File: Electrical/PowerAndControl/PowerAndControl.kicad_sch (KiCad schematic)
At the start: 21 parts, among them J1 Conn_02x03_Counter_Clockwise, SW2 SW_SPDT_312, U1 MCP73811T-420I-OT, U2 TPS22919QDCKRQ1, U3 TPS3840PL30DBVR

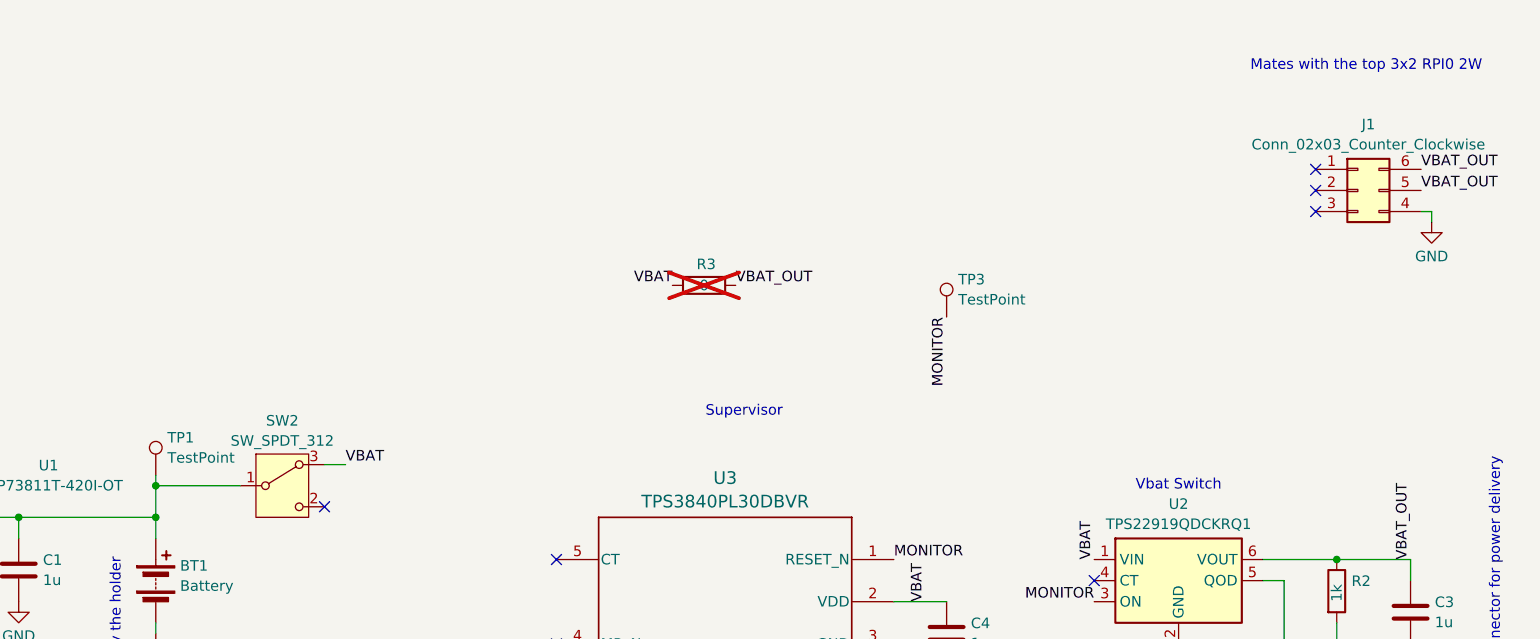
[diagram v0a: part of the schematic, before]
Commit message: Layout of AA variant complete.  Need to check pinout 2x more
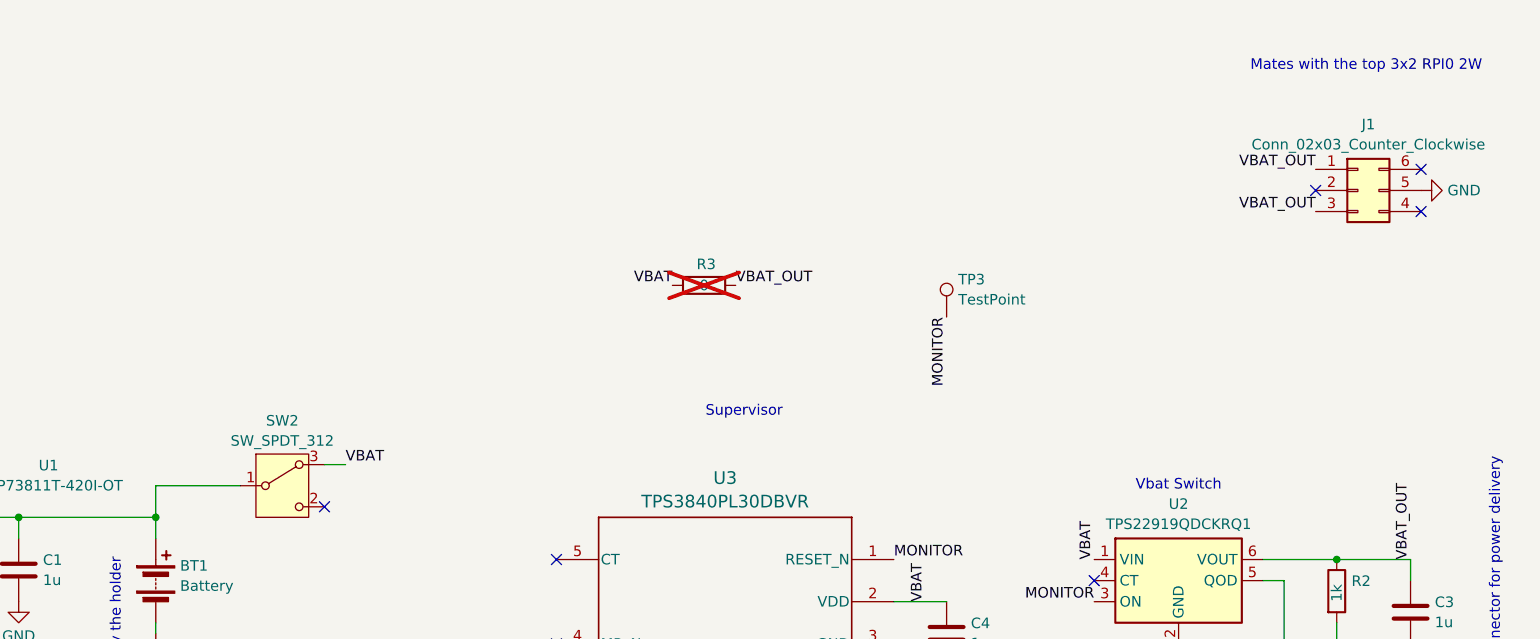
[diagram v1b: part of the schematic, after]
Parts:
- removed TP1: TestPoint, TestPoint:TestPoint_Pad_1.0x1.0mm, symbol Connector:TestPoint
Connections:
- net GND: now also J1.5 (Pin_5); no longer J1.4 (Pin_4)
- net VBAT_OUT: now also J1.1 (Pin_1), J1.3 (Pin_3); no longer J1.5 (Pin_5), J1.6 (Pin_6)
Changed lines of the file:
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@@
-		(color 0 0 0 0)
-	)
-	(junction
-		(at 115.57 107.95)
-		(diameter 0)
 		(color 0 0 0 0)
 	)
@@
 	)
 	(no_connect
-		(at 255.27 72.39)
-	)
-	(no_connect
 		(at 135.89 110.49)
 	)
@@
 	)
 	(no_connect
-		(at 255.27 69.85)
+		(at 267.97 74.93)
 	)
 	(no_connect
@@
 	)
 	(no_connect
-		(at 255.27 74.93)
+		(at 255.27 72.39)
 	)
 	(no_connect
@@
 	)
 	(no_connect
+		(at 267.97 69.85)
+	)
+	(no_connect
 		(at 163.83 116.84)
 	)
@@
 	(wire
 		(pts
-			(xy 269.24 74.93) (xy 269.24 76.2)
-		)
-		(stroke
-			(width 0)
-			(type default)
-		)
-	)
-	(wire
-		(pts
 			(xy 266.7 116.84) (xy 266.7 119.38)
 		)
@@
 	(wire
 		(pts
-			(xy 115.57 106.68) (xy 115.57 107.95)
-		)
-		(stroke
-			(width 0)
-			(type default)
-		)
-	)
-	(wire
-		(pts
 			(xy 43.18 97.79) (xy 43.18 95.25)
 		)
@@
 		(pts
 			(xy 138.43 105.41) (xy 135.89 105.41)
-		)
-		(stroke
-			(width 0)
-			(type default)
-		)
-	)
-	(wire
-		(pts
-			(xy 267.97 74.93) (xy 269.24 74.93)
 		)
 		(stroke
@@
 		)
 	)
-	(label "VBAT_OUT"
-		(at 267.97 72.39 0)
-		(effects
-			(font
-				(size 1.27 1.27)
-			)
-			(justify left bottom)
-		)
-	)
 	(label "VBAT"
 		(at 208.28 121.92 90)
@@
 		)
 	)
+	(label "VBAT_OUT"
+		(at 255.27 69.85 180)
+		(effects
+			(font
+				(size 1.27 1.27)
+			)
+			(justify right bottom)
+		)
+	)
+	(label "VBAT_OUT"
+		(at 255.27 74.93 180)
+		(effects
+			(font
+				(size 1.27 1.27)
+			)
+			(justify right bottom)
+		)
+	)
 	(label "MONITOR"
 		(at 204.47 116.84 0)
@@
 		)
 	)
-	(label "VBAT_OUT"
-		(at 267.97 69.85 0)
-		(effects
-			(font
-				(size 1.27 1.27)
-			)
-			(justify left bottom)
-		)
-	)
 	(symbol
 		(lib_id "power:GND")
@@
 	(symbol
 		(lib_id "power:GND")
-		(at 269.24 76.2 0)
+		(at 267.97 72.39 90)
 		(unit 1)
 		(exclude_from_sim no)
@@
 		(fields_autoplaced yes)
 		(property "Reference" "#PWR017"
-			(at 269.24 82.55 0)
+			(at 274.32 72.39 0)
 			(effects
 				(font
@@
 		)
 		(property "Value" "GND"
-			(at 269.24 80.3331 0)
-			(effects
-				(font
-					(size 1.27 1.27)
-				)
+			(at 271.145 72.39 90)
+			(effects
+				(font
+					(size 1.27 1.27)
+				)
+				(justify right)
 			)
 		)
 		(property "Footprint" ""
-			(at 269.24 76.2 0)
+			(at 267.97 72.39 0)
 			(effects
 				(font
@@
 		)
 		(property "Datasheet" ""
-			(at 269.24 76.2 0)
+			(at 267.97 72.39 0)
 			(effects
 				(font
@@
 		)
 		(property "Description" "Power symbol creates a global label with name \"GND\" , ground"
-			(at 269.24 76.2 0)
-			(effects
-				(font
-					(size 1.27 1.27)
-				)
-				(hide yes)
-			)
-		)
-		(pin "1"
-		)
-		(instances
-			(project ""
+			(at 267.97 72.39 0)
+			(effects
+				(font
+					(size 1.27 1.27)
+				)
+				(hide yes)
+			)
+		)
+		(pin "1"
+		)
+		(instances
+			(project "PowerAndControl"
 				(path "/a4a2b9eb-fb12-482a-8327-284239d2fb85"
 					(reference "#PWR017")
 					(unit 1)
 				)
-			)
-		)
-	)
-	(symbol
-		(lib_id "Connector:TestPoint")
-		(at 115.57 106.68 0)
-		(unit 1)
-		(exclude_from_sim no)
-		(in_bom yes)
-		(on_board yes)
-		(dnp no)
-		(property "Reference" "TP1"
-			(at 116.967 102.1658 0)
-			(effects
-				(font
-					(size 1.27 1.27)
-				)
-				(justify left)
-			)
-		)
-		(property "Value" "TestPoint"
-			(at 116.967 104.5901 0)
-			(effects
-				(font
-					(size 1.27 1.27)
-				)
-				(justify left)
-			)
-		)
-		(property "Footprint" "TestPoint:TestPoint_Pad_1.0x1.0mm"
-			(at 120.65 106.68 0)
-			(effects
-				(font
-					(size 1.27 1.27)
-				)
-				(hide yes)
-			)
-		)
-		(property "Datasheet" "~"
-			(at 120.65 106.68 0)
-			(effects
-				(font
-					(size 1.27 1.27)
-				)
-				(hide yes)
-			)
-		)
-		(property "Description" "test point"
-			(at 115.57 106.68 0)
-			(effects
-				(font
-					(size 1.27 1.27)
-				)
-				(hide yes)
-			)
-		)
-		(pin "1"
-		)
-		(instances
-			(project ""
-				(path "/a4a2b9eb-fb12-482a-8327-284239d2fb85"
-					(reference "TP1")
-					(unit 1)
-				)

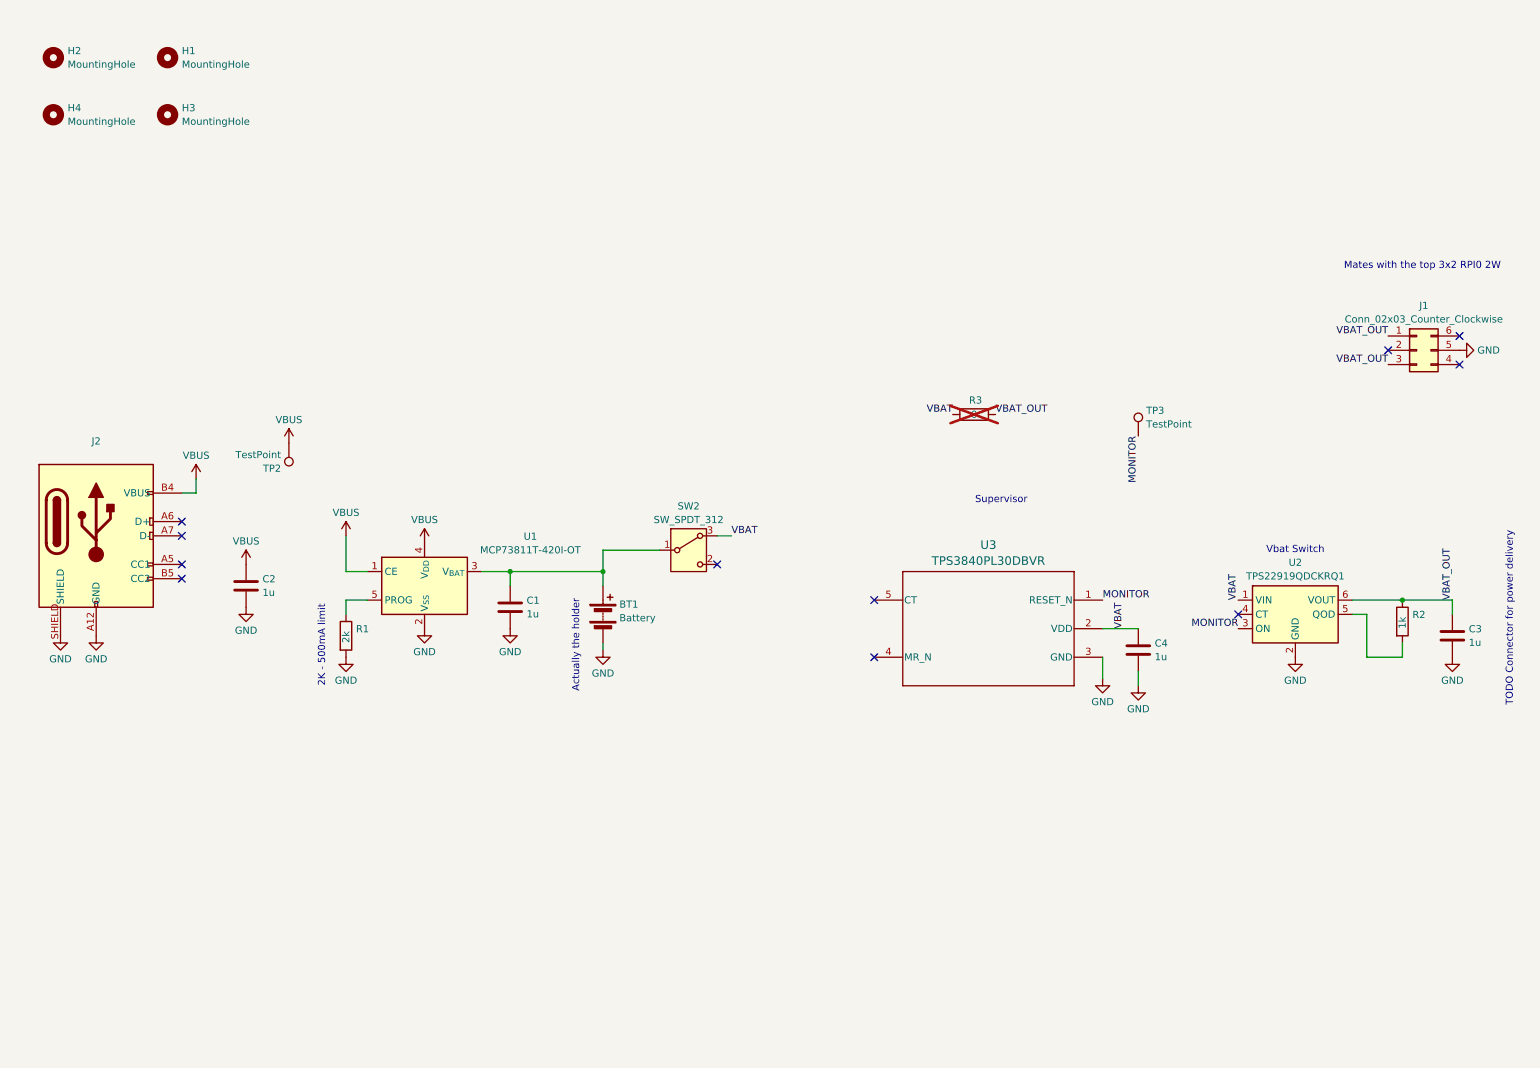
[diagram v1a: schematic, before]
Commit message: Cleaner Schematic / LED Indicators, better Layout
Added 3 LEDs for indicators.
Shcematic Cleaned up in general.
New Charger component
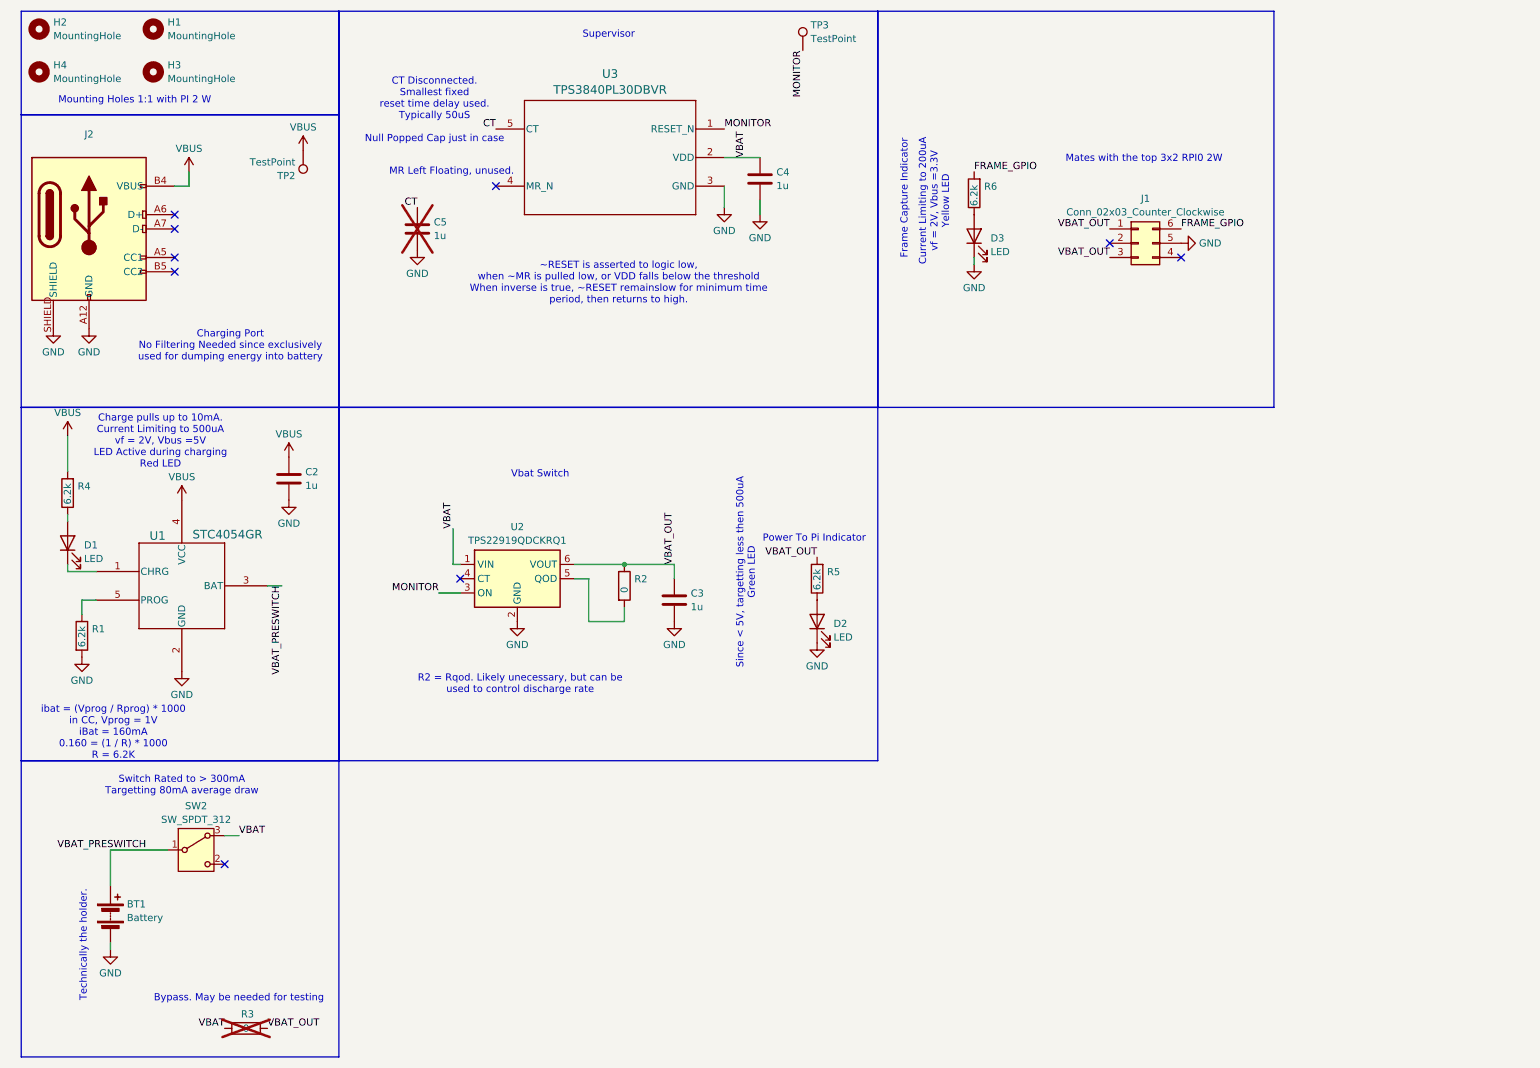
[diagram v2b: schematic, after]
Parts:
- removed C1: 1u, Capacitor_SMD:C_0402_1005Metric_Pad0.74x0.62mm_HandSolder, symbol Device:C
- removed U1: MCP73811T-420I-OT, Package_TO_SOT_SMD:SOT-23-5, symbol Battery_Management:MCP73811T-420I-OT
- added C5: 1u, Capacitor_SMD:C_0603_1608Metric_Pad1.08x0.95mm_HandSolder, symbol Device:C
- added D1, D2, D3: LED, Library:LED_0604, symbol Device:LED
- added R4, R5, R6: 6.2k, Resistor_SMD:R_0402_1005Metric_Pad0.72x0.64mm_HandSolder, symbol Device:R
- added U1: STC4054GR, Package_TO_SOT_SMD:TSOT-23-5_HandSoldering, symbol New_Library:STC4054GR
- BT1: MPN  (none) -> BAT_BK-53
- R1: value 2k -> 6.2k
- R2: value 1k -> 0
- SW2: MPN (none) -> EGJ1210
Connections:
- net GND: now also C5.2, D2.1 (K), D3.1 (K), U1.2 (GND)
- net VBAT_OUT: now also R5.2
- net VBUS: now also R4.2, U1.4 (VCC)
- net at R1.1: now also U1.5 (PROG)
- net FRAME_GPIO: now reaches J1.6 (Pin_6)
- net FRAME_GPIO: now also R6.2
- net CT: now reaches U3.5 (CT)
- net CT: now also C5.1
- net VBAT_PRESWITCH: now reaches BT1.1 (+), SW2.1 (B)
- net VBAT_PRESWITCH: now also U1.3 (BAT)
- new net: D1.1 (K), U1.1 (CHRG)
- new net: D1.2 (A), R4.1
- new net: D3.2 (A), R6.1
- new net: D2.2 (A), R5.1
- no-connect marks 11 -> 9
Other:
- note added: "Bypass. May be needed for testing"
- note added: "CT Disconnected. Smallest fixed reset time delay used. Typically 50uS Null Popped Cap just in case"
- note added: "Charge pulls up to 10mA. Current Limiting to 500uA vf = 2V, Vbus =5V LED Active during charging Red LED"
- note added: "Charging Port No Filtering Needed since exclusively used for dumping energy into battery"
- note added: "Current Limiting to 200uA vf = 2V, Vbus =3.3V Yellow LED"
- note added: "Frame Capture Indicator"
- note added: "MR Left Floating, unused."
- note added: "Mounting Holes 1:1 with PI 2 W"
- note added: "Power To Pi Indicator"
- note added: "R2 = Rqod. Likely unecessary, but can be used to control discharge rate"
- note added: "Since < 5V, targetting less then 500uA Green LED"
- note added: "Switch Rated to > 300mA Targetting 80mA average draw"
- note added: "Technically the holder."
- note added: "ibat = (Vprog / Rprog) * 1000 in CC, Vprog = 1V iBat = 160mA 0.160 = (1 / R) * 1000 R = 6.2K"
- note added: "~RESET is asserted to logic low, when ~MR is pulled low, or VDD falls below the threshold When inverse is true, ~RESET remainslow for minimum time period, then returns to high."
- note removed: "2K - 500mA limit"
- note removed: "Actually the holder"
- note removed: "TODO Connector for power delivery"
- moved on the sheet: BT1, C2, C3, C4, H1, H2, H3, H4, J1, J2, R2, R3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
